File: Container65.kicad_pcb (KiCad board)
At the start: 2 copper layers, 78.7 x 115.9 mm, 97 parts, among them J1 Conn_01x03, J3 POGOm1, J4 POGOm2, J5 POGOf1, J6 POGOf2, SW1 RotaryEncoder_Switch, U1 RP2040, U2 TYPE-C-31-M-12, U3 XC6206PxxxMR, U4 W25Q128JVS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

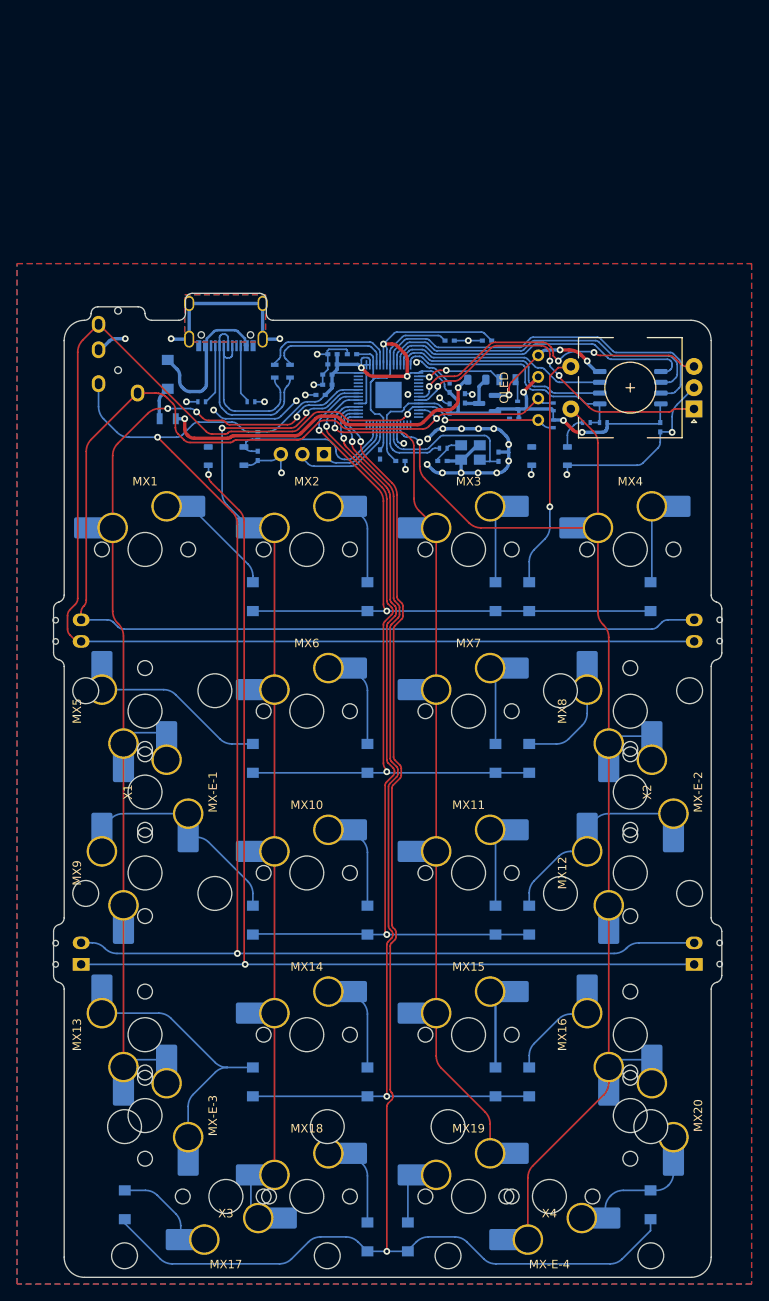
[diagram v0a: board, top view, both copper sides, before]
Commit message: Add eblaster lib
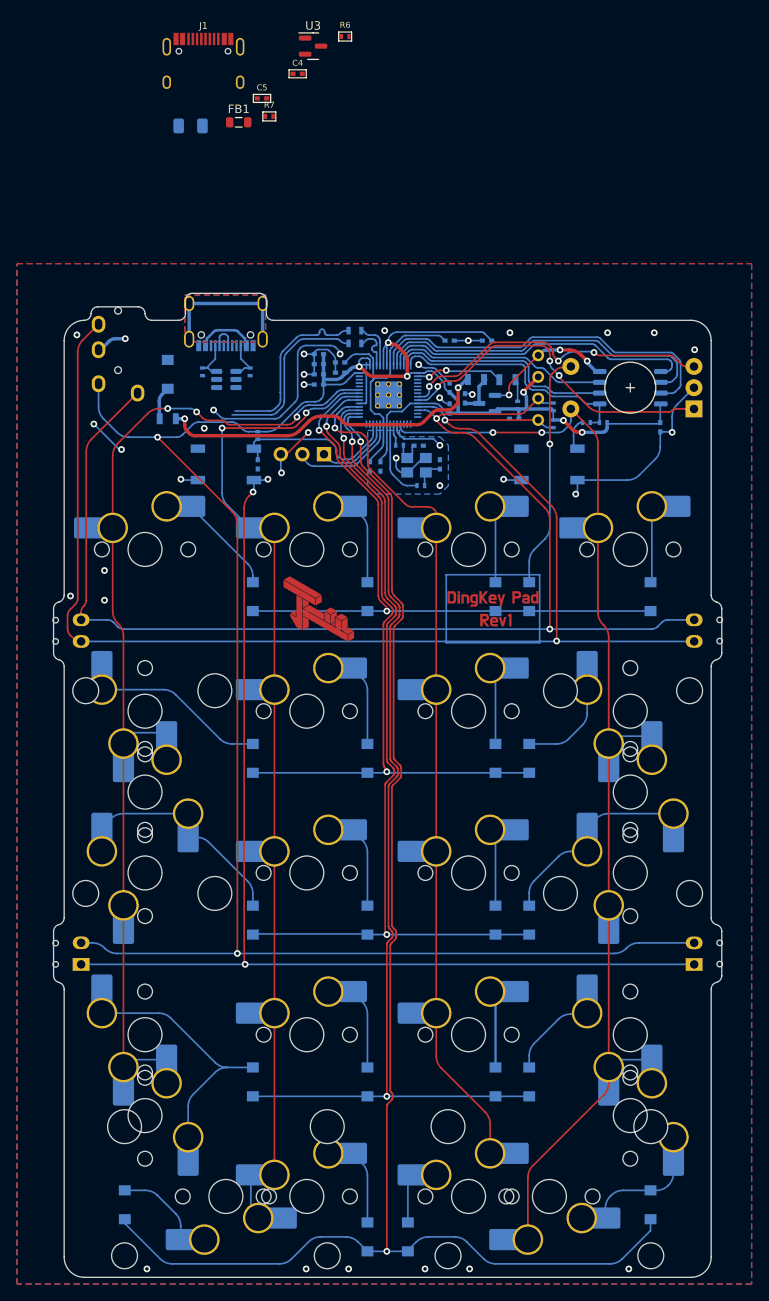
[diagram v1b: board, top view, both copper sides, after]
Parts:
- added #G***: LOGO, Extras:DingKeyF.Mask, F.Cu at (69.7, 55.4)
- added #G***: LOGO, Extras:DingKeyF.Cu, F.Cu at (69.7, 55.4)
- added C4: 1uF, Keebio-Parts:C_0402, F.Cu at (67.2, -7.60)
- added C5: 1uF, Keebio-Parts:C_0402, F.Cu at (63.0, -4.70)
- added DV1: Schottky, Fuse:Fuse_1206_3216Metric, B.Cu at (54.6, -1.46)
- added F1: 500mA, Keebio-Parts:Fuse_0805, B.Cu at (88.2, 28.4)
- added G*** (x2): LOGO, LOGO, F.Cu at (90.2, 55.4)
- added J1: TYPE-C-31-M-12, Keebio-Parts:HRO-TYPE-C-31-M-12-Assembly, F.Cu at (56.1, -4.00)
- added R12: 1k ohm, Keebio-Parts:R_0402, B.Cu at (79.2, 36.1)
- added R6: 5.1k, Keebio-Parts:R_0402, F.Cu at (72.8, -12.0)
- added R7: 5.1k, Keebio-Parts:R_0402, F.Cu at (63.8, -2.58)
- added REF**: graphic-rp2040, Extras:graphic-rp2040, B.Cu at (82.7, 25.4)
- added REF**: graphic-flashmem, Extras:graphic-flashmem, B.Cu at (109.9, 25.6)
- added REF**: graphic-crystal-4pin, Extras:graphic-crystal-4pin, B.Cu at (86.2, 38.4)
- added U2: SRV05-4, Package_TO_SOT_SMD:SOT-23-6, B.Cu at (58.8, 28.4)
- added U3: XC6206PxxxMR, Package_TO_SOT_SMD:SOT-23, F.Cu at (69.0, -10.9)
- D22: value Power LED (Blue) -> LED
- FB1: value 100@100MHz -> (10-50)@100MHz; moved to F.Cu
- U1: footprint Extras:rp2040 -> Keebio-Parts:RP2040-QFN-56
- U5, U6: footprint Extras:3x4x2.5mm Micro Switch -> Extras:tactile-switch
- moved FB1 41.3 mm to (60.2, -1.89)
- moved R1 10.6 mm to (73.9, 22.6), turned to 180 degrees
- moved C6 9.49 mm to (81.4, 36.2), turned to 0 degrees
- moved R2 8.32 mm to (73.9, 24.1), turned to 180 degrees
- moved Y1 6.52 mm to (81.2, 38.5), turned to 0 degrees
- moved R3 5.14 mm to (81.7, 40.9)
- moved R6 3.53 mm to (61.6, 27.5), turned to -90 degrees
- moved R7 3.53 mm to (56.0, 27.5), turned to -90 degrees
- moved C11 2.44 mm to (76.9, 38.6), turned to -90 degrees
- moved C17 1.86 mm to (75.7, 38.6)
- moved C2 1.71 mm to (72.2, 26.4)
- moved C8 1.60 mm to (69.7, 25.4)
- moved C15 1.58 mm to (69.7, 27.8)
- moved C9 1.58 mm to (69.7, 26.6)
- moved C1 1.33 mm to (72.2, 27.6)
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- renumbered J1 to J2
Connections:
- C6 pad 1: OSC_OUT -> Net-(C6-Pad1)
- FB1 pad 1: Net-(F1-Pad2) -> VBUS
- FB1 pad 2: +5V -> Net-(FB1-Pad2)
- Y1 pad 1: OSC_OUT -> Net-(C6-Pad1)
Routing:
- net OSC_OUT: track 19.3 -> 2.57 mm
- net SDA: track 173.9 -> 161.6 mm
- net GND: track 274.0 -> 261.9 mm, vias 38 -> 43
- net VBUS: track 19.1 -> 7.22 mm
- net USB_MCU+: track 16.2 -> 5.71 mm
- net SCL: track 160.3 -> 151.0 mm, vias 1 -> 2
- net USB_MCU-: track 14.7 -> 5.67 mm
- net COL3: track 144.7 -> 136.9 mm, vias 1 -> 2
- net +1V1: track 27.2 -> 30.7 mm
- net Net-(C6-Pad1): track 0.00 -> 3.53 mm
- net +3V3: track 281.6 -> 284.6 mm
- net CC2: track 6.91 -> 4.91 mm
- net USB-: track 21.8 -> 23.8 mm
- net CC1: track 7.11 -> 5.34 mm
- net COL2: track 101.5 -> 100.1 mm
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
